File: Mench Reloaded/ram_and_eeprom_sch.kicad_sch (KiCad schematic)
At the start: 11 parts, among them J1 Conn_01x40_Pin, J3 FTDI serial, J4 Conn_01x40_Pin, J9 RAM CSB select, U2 628128_DIP32_SSOP32, U3 28C256, U4 74HC00, U5 74HC00

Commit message: First draft of PCB
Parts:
- added C1: 0.33uF, Capacitor_SMD:C_0805_2012Metric_Pad1.18x1.45mm_HandSolder, symbol Device:C_Small
- added C4: 0.1uF, Capacitor_SMD:C_0805_2012Metric_Pad1.18x1.45mm_HandSolder, symbol Device:C_Small
- added C7: 10uF, Capacitor_THT:CP_Radial_D10.0mm_P5.00mm, symbol Device:C_Polarized_US
- added D9: LED, LED_SMD:LED_0805_2012Metric_Pad1.15x1.40mm_HandSolder, symbol Device:LED
- added J1: Barrel_Jack_Switch, Connector_BarrelJack:BarrelJack_Horizontal, symbol Connector:Barrel_Jack_Switch
- added R13: 3K, Resistor_SMD:R_0805_2012Metric_Pad1.20x1.40mm_HandSolder, symbol Device:R_Small_US
- added R14: 3K, Resistor_SMD:R_0805_2012Metric_Pad1.20x1.40mm_HandSolder, symbol Device:R_US
- added U1: LM7805_TO220, Package_TO_SOT_THT:TO-220-3_Vertical, symbol Regulator_Linear:LM7805_TO220
- C5, C6: footprint (none) -> Capacitor_SMD:C_0805_2012Metric_Pad1.18x1.45mm_HandSolder
- J1: renamed from J3; footprint (none) -> Connector_PinHeader_2.54mm:PinHeader_1x06_P2.54mm_Horizontal
- J2: renamed from J4; footprint (none) -> Connector_PinHeader_2.54mm:PinHeader_1x40_P2.54mm_Vertical
- J3: renamed from J9; footprint (none) -> Connector_PinHeader_2.54mm:PinHeader_2x04_P2.54mm_Vertical
- J4: renamed from J1; footprint (none) -> Connector_PinHeader_2.54mm:PinHeader_1x40_P2.54mm_Vertical
- U2: value 628128_DIP32_SSOP32 -> 128K RAM; footprint (none) -> Package_DIP:DIP-32_W15.24mm_Socket_LongPads
- U3: footprint (none) -> Package_DIP:DIP-28_W15.24mm_Socket_LongPads
- U5: footprint (none) -> Package_DIP:DIP-14_W7.62mm_Socket_LongPads
- U5: renamed from U4; footprint (none) -> Package_DIP:DIP-14_W7.62mm_Socket_LongPads
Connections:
- net +5V: now also C4.1, C7.1, R13.1, R14.1, U1.3 (VO)
- net A5B: now also J4.35 (Pin_35); no longer J4.34 (Pin_34)
- net BE: now also J4.33 (Pin_33); no longer J4.32 (Pin_32)
- net GND: now also J4.38 (Pin_38), J4.39 (Pin_39), C1.2, C4.2, C7.2, D9.1 (K), J1.2, J1.3, U1.2 (GND)
- net RUN: now also J4.34 (Pin_34); no longer J4.33 (Pin_33)
- net TG0: now also J4.36 (Pin_36); no longer J4.38 (Pin_38)
- net TG1: now also J4.37 (Pin_37); no longer J4.39 (Pin_39)
- net at U2.30 (CS2): now also R13.2
- new net: D9.2 (A), R14.2
- new net: C1.1, J1.1, U1.1 (VI)
- new net BA: J4.32 (Pin_32)

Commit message: Completed initial PCB layout. Commiting because I will try to reduce it to 100mm x 100mm
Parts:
- U1: footprint Package_TO_SOT_THT:TO-220-3_Vertical -> Package_TO_SOT_THT:TO-220-3_Horizontal_TabDown
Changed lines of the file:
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@@
       (effects (font (size 1.27 1.27)))
     )
-    (property "Footprint" "Package_TO_SOT_THT:TO-220-3_Vertical" (at 229.87 102.235 0)
+    (property "Footprint" "Package_TO_SOT_THT:TO-220-3_Horizontal_TabDown" (at 229.87 102.235 0)
       (effects (font (size 1.27 1.27) italic) hide)
     )

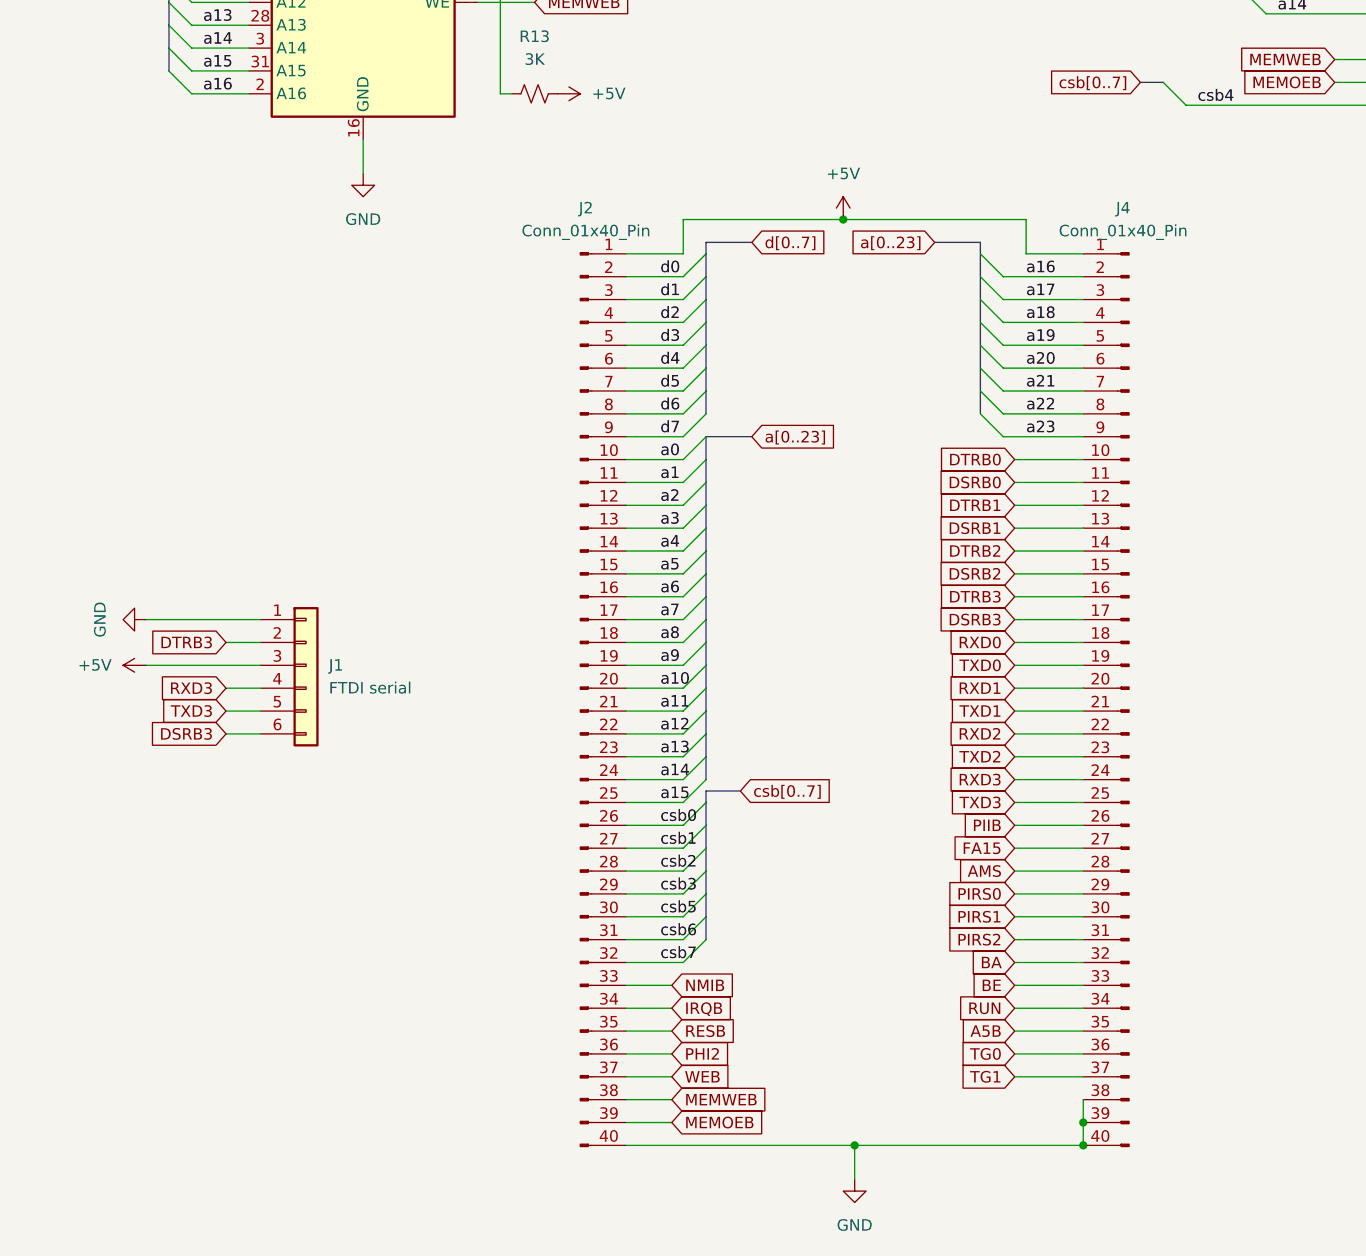
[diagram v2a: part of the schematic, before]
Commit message: Reworked the layout to 100mm by 100mm. Also changed the headers to be compatible with the W65C265SXB.
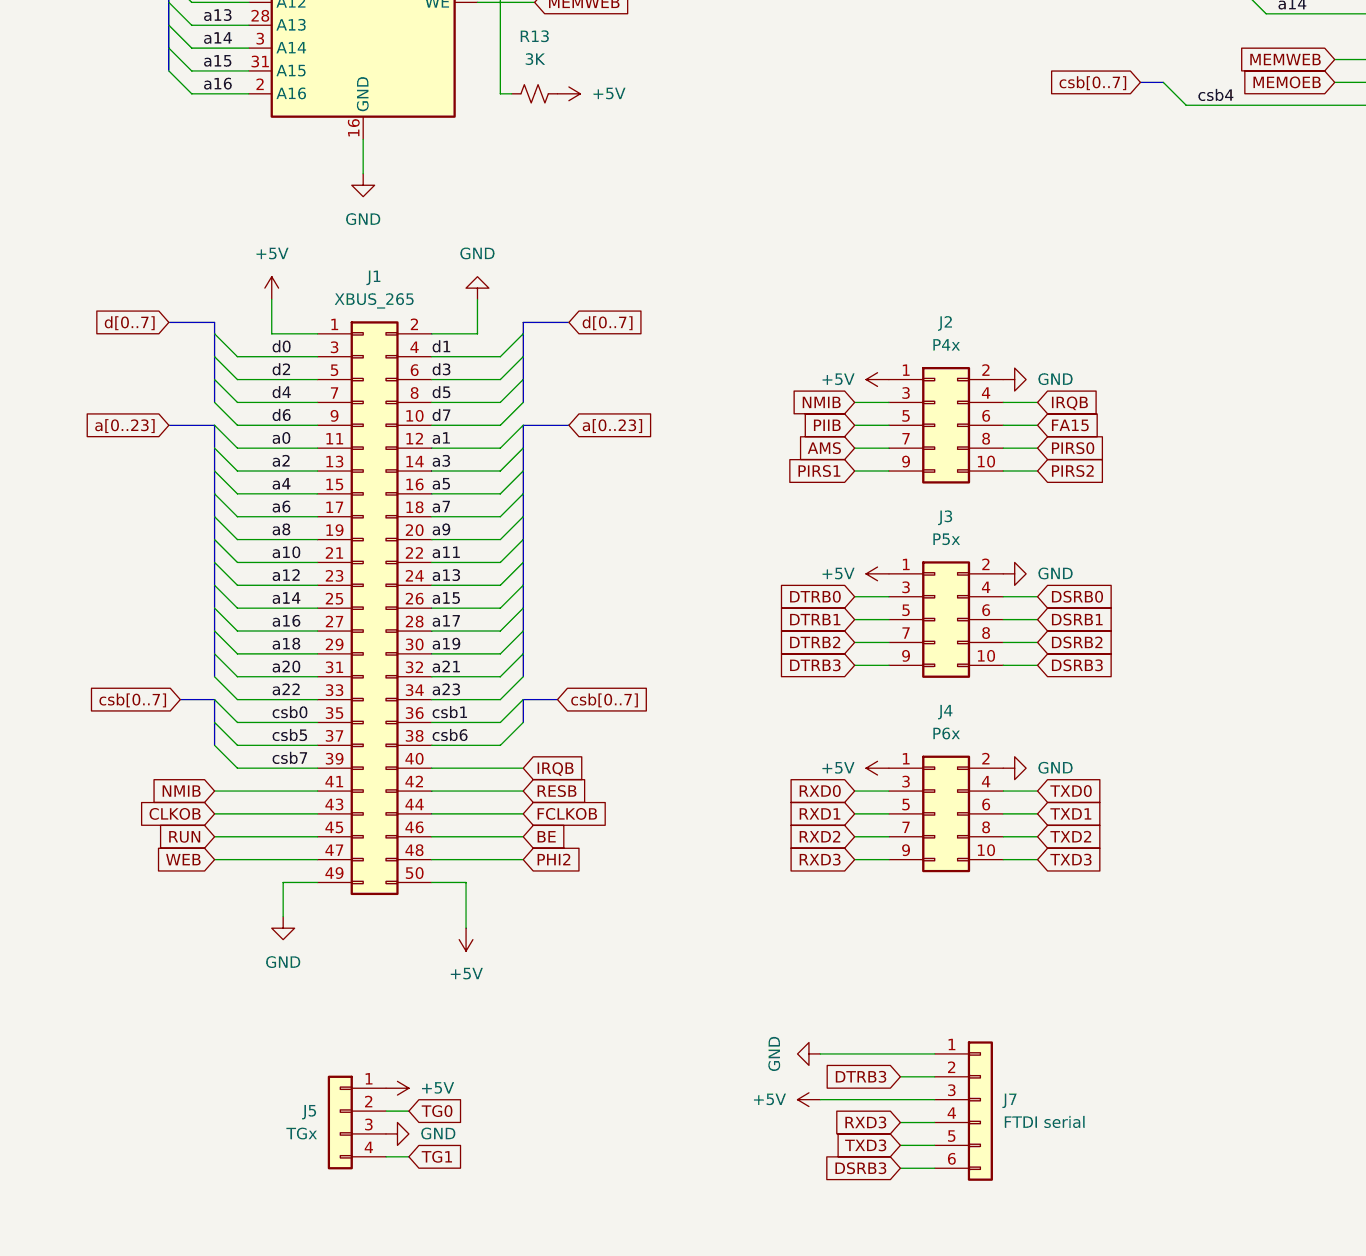
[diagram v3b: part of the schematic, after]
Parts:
- removed J2, J4: Conn_01x40_Pin, Connector_PinHeader_2.54mm:PinHeader_1x40_P2.54mm_Vertical, symbol Connector:Conn_01x40_Pin
- added J1: XBUS_265, Connector_PinHeader_2.54mm:PinHeader_2x25_P2.54mm_Vertical, symbol Connector_Generic:Conn_02x25_Odd_Even
- added J2: P4x, Connector_PinHeader_2.54mm:PinHeader_2x05_P2.54mm_Vertical, symbol Connector_Generic:Conn_02x05_Odd_Even
- added J3: P5x, Connector_PinHeader_2.54mm:PinHeader_2x05_P2.54mm_Vertical, symbol Connector_Generic:Conn_02x05_Odd_Even
- added J4: P6x, Connector_PinHeader_2.54mm:PinHeader_2x05_P2.54mm_Vertical, symbol Connector_Generic:Conn_02x05_Odd_Even
- added J5: TGx, Connector_PinHeader_2.54mm:PinHeader_1x04_P2.54mm_Vertical, symbol Connector_Generic:Conn_01x04
- C7: footprint Capacitor_THT:CP_Radial_D10.0mm_P5.00mm -> Capacitor_THT:CP_Radial_D5.0mm_P2.50mm
- renumbered J1 to J7
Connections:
- net +5V: now also J1.1 (Pin_1), J1.50 (Pin_50), J2.1 (Pin_1), J3.1 (Pin_1), J4.1 (Pin_1), J5.1 (Pin_1)
- net AMS: now also J2.7 (Pin_7)
- net BE: now also J1.46 (Pin_46)
- net DSRB0: now also J3.4 (Pin_4)
- net DSRB1: now also J3.6 (Pin_6)
- net DSRB2: now also J3.8 (Pin_8)
- net DSRB3: now also J3.10 (Pin_10)
- net DTRB0: now also J3.3 (Pin_3)
- net DTRB1: now also J3.5 (Pin_5)
- net DTRB2: now also J3.7 (Pin_7)
- net DTRB3: now also J3.9 (Pin_9)
- net FA15: now also J2.6 (Pin_6)
- net GND: now also J1.2 (Pin_2), J1.49 (Pin_49), J2.2 (Pin_2), J3.2 (Pin_2), J4.2 (Pin_2), J5.3 (Pin_3)
- net IRQB: now also J1.40 (Pin_40), J2.4 (Pin_4)
- net NMIB: now also J1.41 (Pin_41), J2.3 (Pin_3)
- net PHI2: now also J1.48 (Pin_48)
- net PIIB: now also J2.5 (Pin_5)
- net PIRS0: now also J2.8 (Pin_8)
- net PIRS1: now also J2.9 (Pin_9)
- net PIRS2: now also J2.10 (Pin_10)
- net RESB: now also J1.42 (Pin_42)
- net RUN: now also J1.45 (Pin_45)
- net RXD0: now also J4.3 (Pin_3)
- net RXD1: now also J4.5 (Pin_5)
- net RXD2: now also J4.7 (Pin_7)
- net RXD3: now also J4.9 (Pin_9)
- net TG0: now also J5.2 (Pin_2)
- net TG1: now also J5.4 (Pin_4)
- net TXD0: now also J4.4 (Pin_4)
- net TXD1: now also J4.6 (Pin_6)
- net TXD2: now also J4.8 (Pin_8)
- net TXD3: now also J4.10 (Pin_10)
- net WEB: now also J1.47 (Pin_47)
- net a0: now also J1.11 (Pin_11)
- net a1: now also J1.12 (Pin_12)
- net a10: now also J1.21 (Pin_21)
- net a11: now also J1.22 (Pin_22)
- net a12: now also J1.23 (Pin_23)
- net a13: now also J1.24 (Pin_24)
- net a14: now also J1.25 (Pin_25)
- net a15: now also J1.26 (Pin_26)
- net a16: now also J1.27 (Pin_27)
- net a17: now also J1.28 (Pin_28)
- net a18: now also J1.29 (Pin_29)
- net a19: now also J1.30 (Pin_30)
- net a2: now also J1.13 (Pin_13)
- net a20: now also J1.31 (Pin_31)
- net a21: now also J1.32 (Pin_32)
- net a22: now also J1.33 (Pin_33)
- net a23: now also J1.34 (Pin_34)
- net a3: now also J1.14 (Pin_14)
- net a4: now also J1.15 (Pin_15)
- net a5: now also J1.16 (Pin_16)
- net a6: now also J1.17 (Pin_17)
- net a7: now also J1.18 (Pin_18)
- net a8: now also J1.19 (Pin_19)
- net a9: now also J1.20 (Pin_20)
- net csb0: now also J1.35 (Pin_35)
- net csb1: now also J1.36 (Pin_36)
- net csb5: now also J1.37 (Pin_37)
- net csb6: now also J1.38 (Pin_38)
- net csb7: now also J1.39 (Pin_39)
- net d0: now also J1.3 (Pin_3)
- net d1: now also J1.4 (Pin_4)
- net d2: now also J1.5 (Pin_5)
- net d3: now also J1.6 (Pin_6)
- net d4: now also J1.7 (Pin_7)
- net d5: now also J1.8 (Pin_8)
- net d6: now also J1.9 (Pin_9)
- net d7: now also J1.10 (Pin_10)
- new net CLKOB: J1.43 (Pin_43)
- new net FCLKOB: J1.44 (Pin_44)
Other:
- moved on the sheet: J7

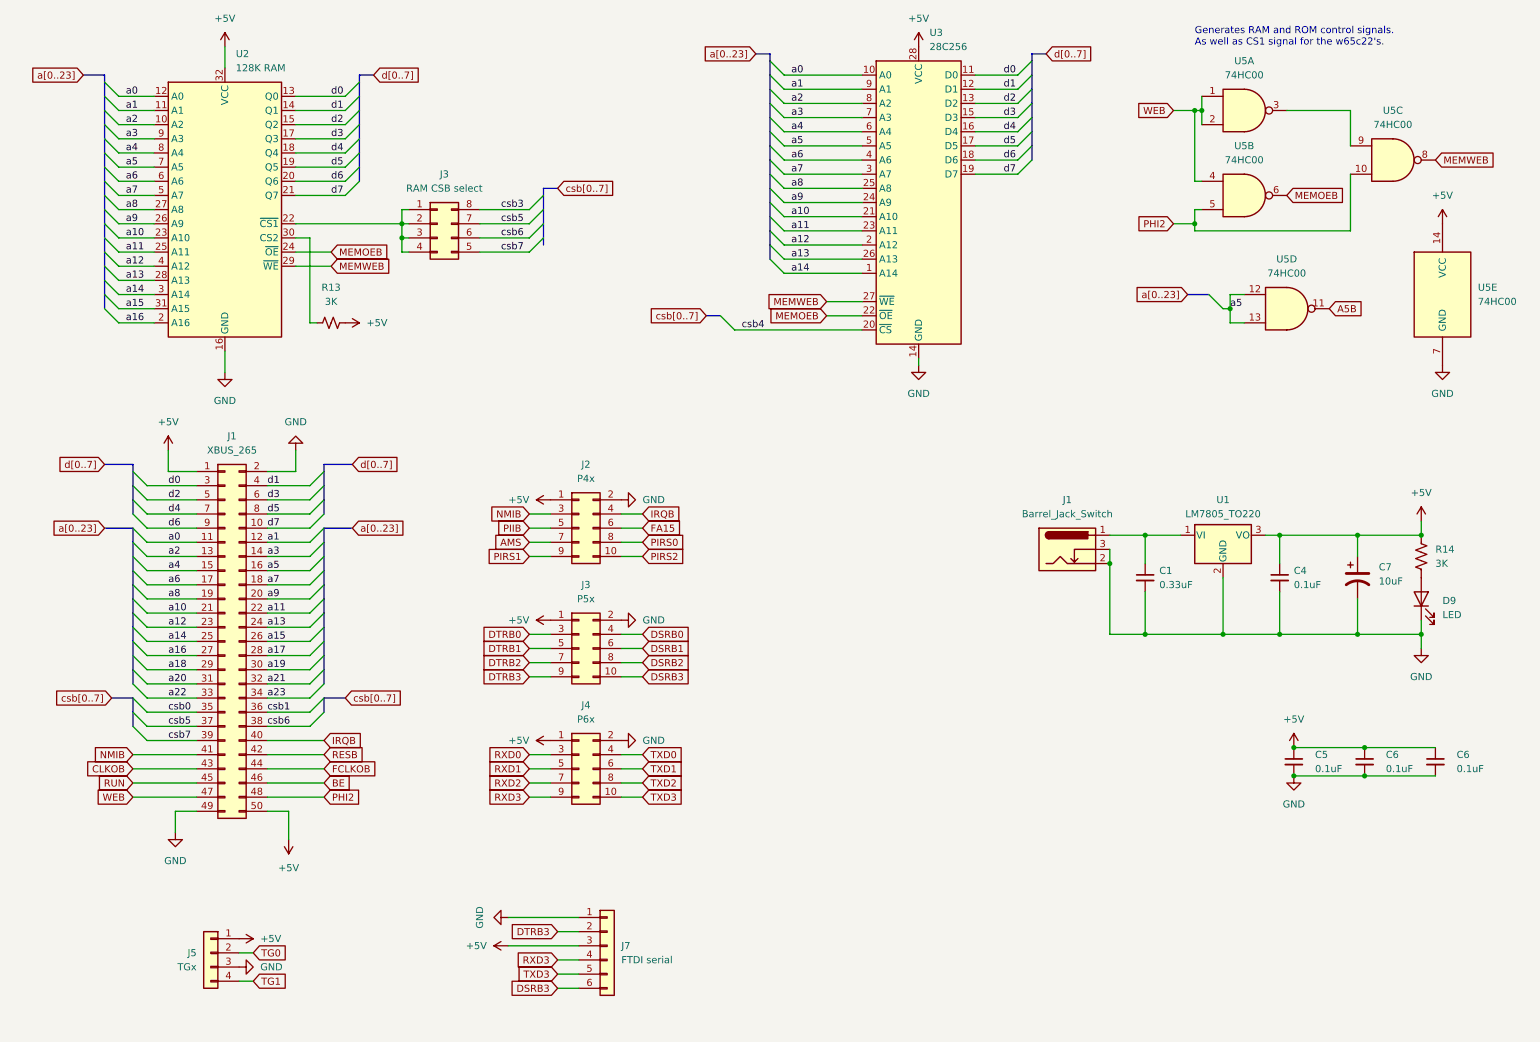
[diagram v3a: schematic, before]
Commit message: Increased the vertical spacing of the components. Aligned the 0-volt pins of the RAM and ROM. Made sure that no resistors or diodes are in the parallel feed area. Removed the unused chip select indicator diodes. I can add them to any cards that use the expansion header. Moved the interrupt select header and diode above the 65c22 because that area was available. For the 65c22 chip I used a5b for cs1 and cs1b for cs2b. This should map it to 0xDFC0.
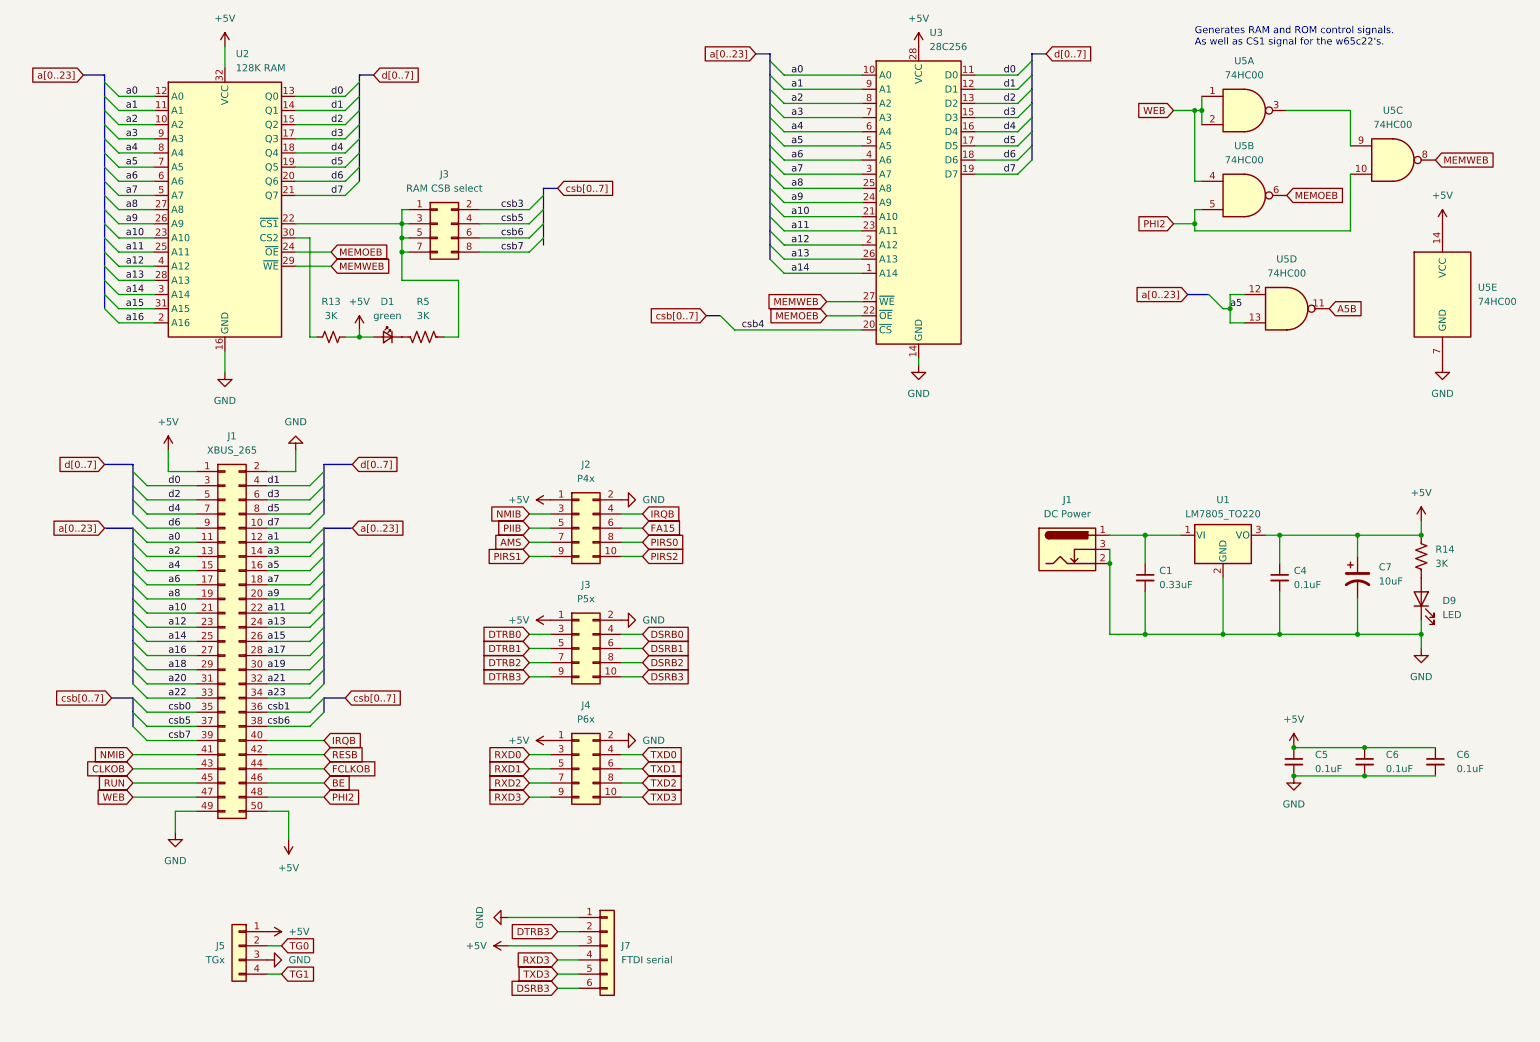
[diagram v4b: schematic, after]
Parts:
- added D1: green, LED_SMD:LED_0805_2012Metric_Pad1.15x1.40mm_HandSolder, symbol Device:LED_Small
- added R5: 3K, Resistor_SMD:R_0805_2012Metric_Pad1.20x1.40mm_HandSolder, symbol Device:R_US
- J1: value Barrel_Jack_Switch -> DC Power
- J3: symbol Connector_Generic:Conn_02x04_Counter_Clockwise -> Connector_Generic:Conn_02x04_Odd_Even
- U5: footprint Package_DIP:DIP-14_W7.62mm_Socket_LongPads -> Package_SO:SOIC-14_3.9x8.7mm_P1.27mm
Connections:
- net +5V: now also D1.2 (A)
- net csb3: now also J3.2 (Pin_2); no longer J3.8 (Pin_8)
- net csb5: now also J3.4 (Pin_4); no longer J3.7 (Pin_7)
- net csb7: now also J3.8 (Pin_8); no longer J3.5 (Pin_5)
- net at J3.1 (Pin_1), J3.3 (Pin_3), U2.22 (~{CS1}): now also J3.5 (Pin_5), J3.7 (Pin_7), R5.1; no longer J3.2 (Pin_2), J3.4 (Pin_4)
- new net: D1.1 (K), R5.2
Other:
- moved on the sheet: J5, R13
